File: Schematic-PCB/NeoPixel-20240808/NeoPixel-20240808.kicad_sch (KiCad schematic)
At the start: 33 parts, among them J1 Conn_01x05_Pin

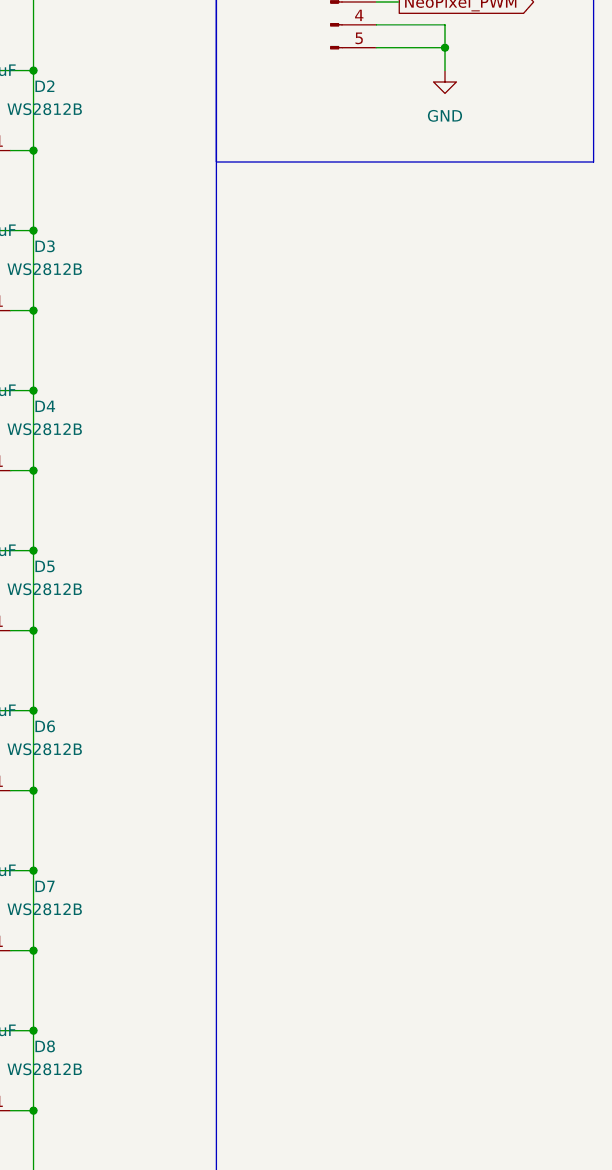
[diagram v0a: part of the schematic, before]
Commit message: update: メイン基板とNeoPixel基板の発注用ファイルを出力したりした
NeoPixel基板はコネクタを1コ→3コに増やした
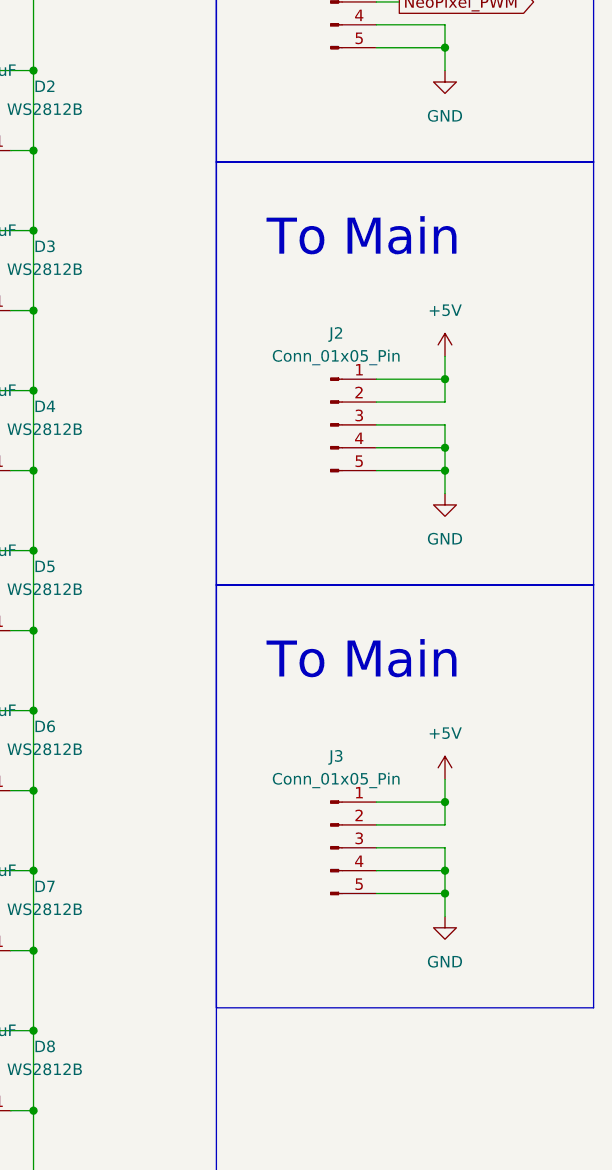
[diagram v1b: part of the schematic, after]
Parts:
- added J2, J3: Conn_01x05_Pin, @2024TOINIOT2-NeoPixel:Connector, symbol Connector:Conn_01x05_Pin
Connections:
- net +5V: now also J2.1 (Pin_1), J2.2 (Pin_2), J3.1 (Pin_1), J3.2 (Pin_2)
- net GND: now also J2.3 (Pin_3), J2.4 (Pin_4), J2.5 (Pin_5), J3.3 (Pin_3), J3.4 (Pin_4), J3.5 (Pin_5)
